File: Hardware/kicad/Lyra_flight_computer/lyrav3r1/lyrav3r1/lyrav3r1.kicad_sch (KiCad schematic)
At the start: 86 parts, among them IC1 TESEO-LIV3F, J1 Conn_01x02, J2 Screw_Terminal_01x02, J4 Conn_01x02, J5 Conn_01x05, J7 USB_B_Micro, J8 Screw_Terminal_01x07, Q1 AO3401A, Q10 AO3400A, Q11 Q_NPN_BEC, Q2 AO3400A, Q3 AO3400A, Q4 AO3400A, Q5 AO3400A, Q7 AO3400A, Q8 AO3400A, Q9 AO3400A, U1 E22-900MM22S, U2 BMI088, U3 BMP388, U5 ADXL375BCCZ-RL7, U6 RT9013-33GB_C19268157, U7 WS7916S-6/TR, U8 RP2040, U9 W25Q128JVS, X2 SX1M12.000M10F30TNN

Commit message: sade
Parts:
- added C8, C9: 100n, Capacitor_SMD:C_0402_1005Metric, symbol Device:C_Small
- added U4: LIS3MDLTR, .pretty:LGA-12_L2.0-W2.0-P0.50-BL, symbol .kicad_sym:LIS3MDLTR
- J2: LCSC Part (none) -> C557685
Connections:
- net +3V3: now also C9.1, U4.10 (CS), U4.5 (Vdd), U4.6 (Vdd_IO)
- net +BATT: now also R2.1; no longer R4.1
- net BATT SENSE : now also R2.2, R4.1; no longer R2.1, R4.2
- net GND: now also R4.2, C8.2, C9.2, U4.12 (Res), U4.2 (Res), U4.3 (GND), U4.9 (SD0/SA1); no longer R2.2
- net SCL: now also U4.1 (SCL/SPC)
- net SDA: now also U4.11 (SDA/SDI/SDO)
- new net: C8.1, U4.4 (C1)
- no-connect marks 30 -> 32
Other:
- note added: "MAGNETOMETER"
- moved on the sheet: J8, R1, R2, R4

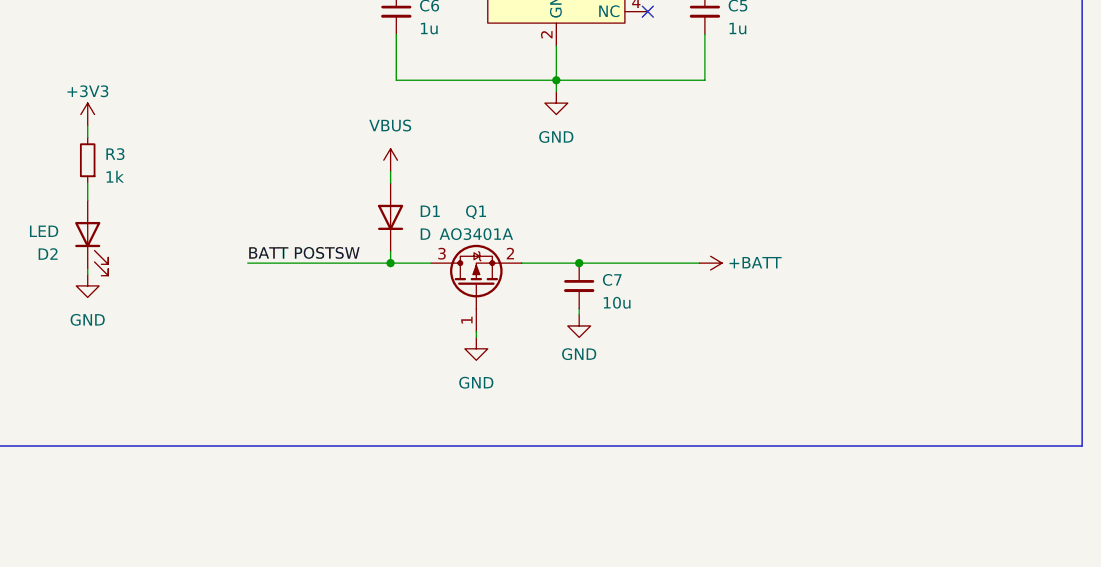
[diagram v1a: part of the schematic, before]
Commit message: added batt protection for lyra, added more parts for reciver
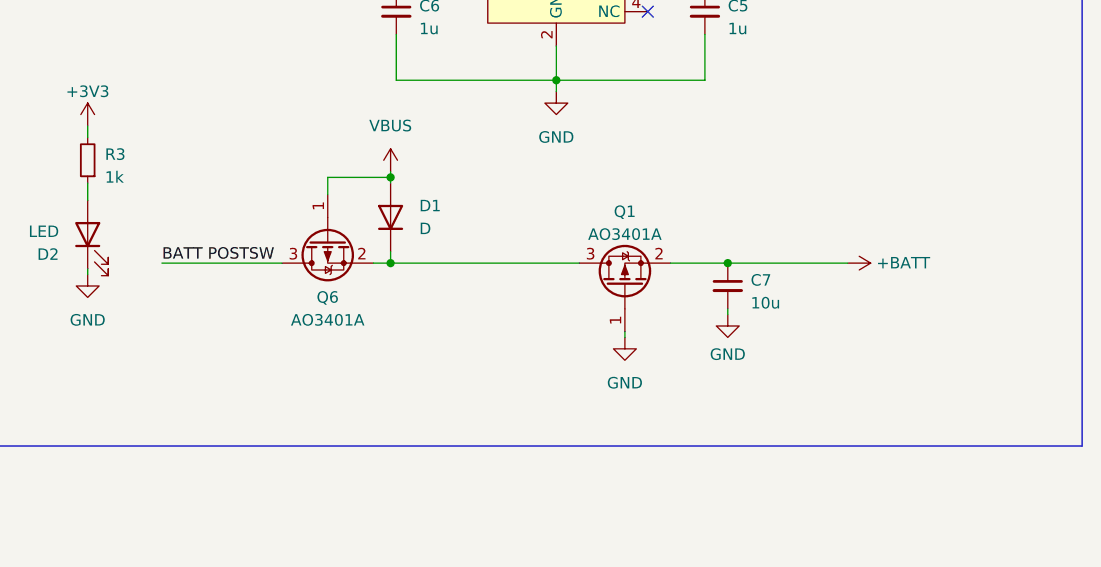
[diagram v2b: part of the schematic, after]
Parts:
- added Q6: AO3401A, Package_TO_SOT_SMD:SOT-23, symbol Transistor_FET:AO3401A
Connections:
- net BATT POSTSW: now also Q6.3 (D); no longer D1.1 (K), Q1.3 (D)
- net VBUS: now also Q6.1 (G)
- new net: D1.1 (K), Q1.3 (D), Q6.2 (S)
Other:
- moved on the sheet: C7, Q1

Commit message: work, lyra mostly final
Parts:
- removed D1: D, Diode_SMD:D_SOD-123, symbol Device:D
- added D1: D_Schottky, Diode_SMD:D_SOD-323F, symbol Device:D_Schottky
- added R5: 100R, Resistor_SMD:R_0402_1005Metric, symbol Device:R_Small
- added R6, R7, R8, R9: 100k, Resistor_SMD:R_0402_1005Metric, symbol Device:R_Small
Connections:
- net +3V3: now also D3.2 (A); no longer D3.1 (K)
- net BUZZER: now also R5.2; no longer Q11.1 (B)
- net GND: now also R6.2, R7.2, R8.2, R9.2
- net P1-: now also R7.1
- net P2-: now also R8.1
- net P3-: now also R6.1
- net P4-: now also R9.1
- net VBUS: now also D1.2 (A)
- net at R28.2: now also D3.1 (K); no longer D3.2 (A)
- net at Q1.3 (D), Q6.2 (S): now also D1.1 (K)
- new net: Q11.1 (B), R5.1
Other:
- moved on the sheet: D3

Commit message: stuffs
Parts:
- removed Q11: Q_NPN_BEC, Package_TO_SOT_SMD:SOT-23, symbol Device:Q_NPN_BEC
- removed R5: 100R, Resistor_SMD:R_0402_1005Metric, symbol Device:R_Small
- R2: value 20k -> 30k; LCSC Part C25765 -> C25105
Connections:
- net +BATT: no longer BZ1.1 (+)
- net BUZZER: now also BZ1.1 (+)
- net GND: now also BZ1.2 (-)

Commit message: post order omcmit
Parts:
- added TP3, TP4, TP5, TP6, TP7: TestPoint, TestPoint:TestPoint_Pad_1.0x1.0mm, symbol Connector:TestPoint
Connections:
- net MISO: now also TP6.1
- net MOSI: now also TP7.1
- net SCK: now also TP5.1
- net SCL: now also TP4.1
- net SDA: now also TP3.1
